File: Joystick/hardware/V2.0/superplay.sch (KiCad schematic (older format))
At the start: 36 parts, among them J1 AVR-PDI-6A, J2 CONN_02X04, J3 USB_B, U1 MCP1700T-3002E, U2 ATXMEGA128A3U-A, U3 TPD4S009DBV, Y1 16MHz

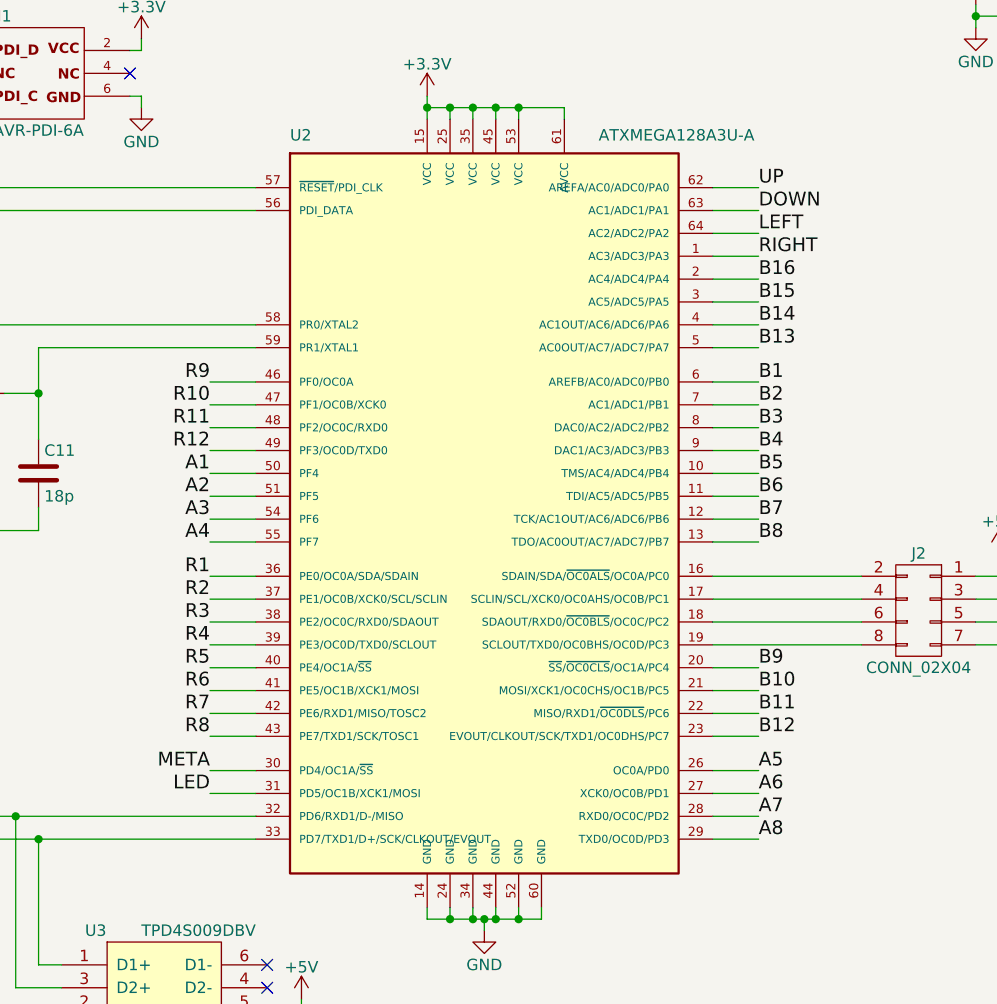
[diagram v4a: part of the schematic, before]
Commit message: Rewired to make PCB layout easier
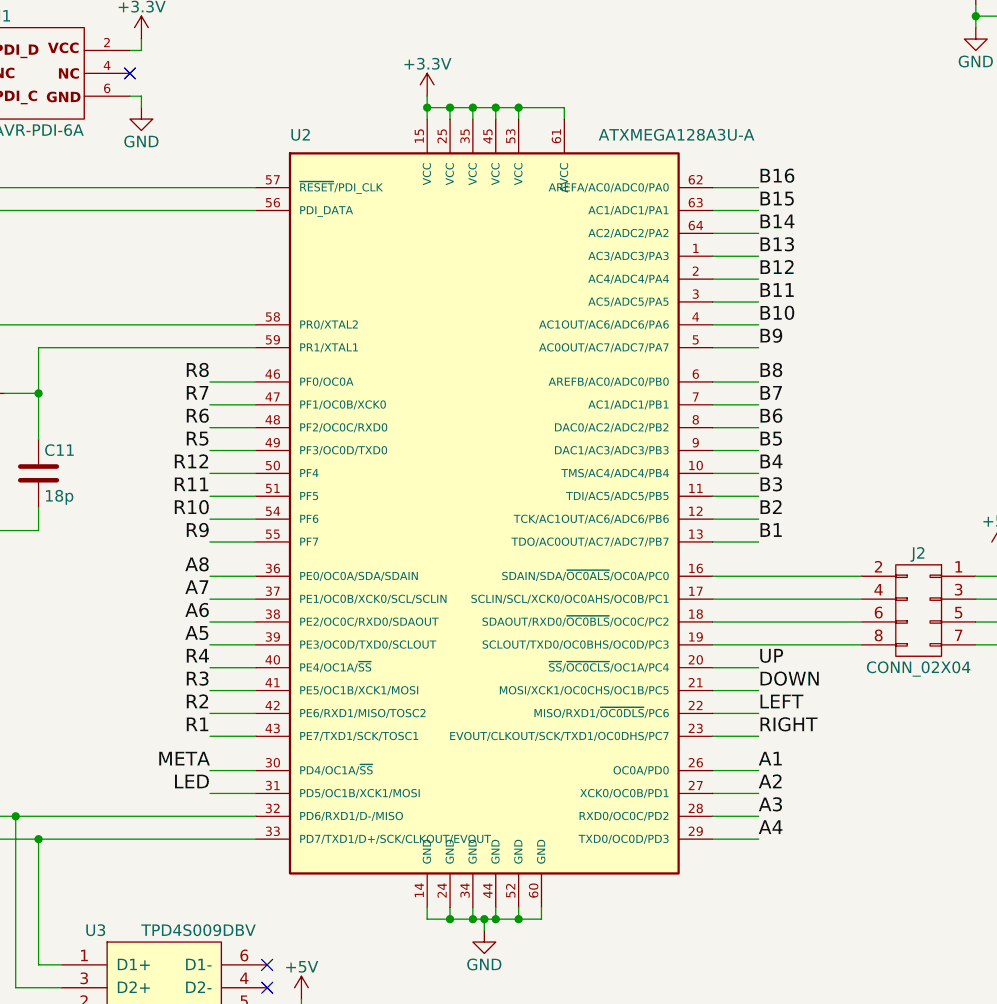
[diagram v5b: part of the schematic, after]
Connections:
- net A1: now also U2.26 (OC0A/PD0); no longer U2.50 (PF4)
- net A2: now also U2.27 (XCK0/OC0B/PD1); no longer U2.51 (PF5)
- net A3: now also U2.28 (RXD0/OC0C/PD2); no longer U2.54 (PF6)
- net A4: now also U2.29 (TXD0/OC0D/PD3); no longer U2.55 (PF7)
- net A5: now also U2.39 (PE3/OC0D/TXD0/SCLOUT); no longer U2.26 (OC0A/PD0)
- net A6: now also U2.38 (PE2/OC0C/RXD0/SDAOUT); no longer U2.27 (XCK0/OC0B/PD1)
- net A7: now also U2.37 (PE1/OC0B/XCK0/SCL/SCLIN); no longer U2.28 (RXD0/OC0C/PD2)
- net A8: now also U2.36 (PE0/OC0A/SDA/SDAIN); no longer U2.29 (TXD0/OC0D/PD3)
- net B1: now also U2.13 (TDO/AC0OUT/AC7/ADC7/PB7); no longer U2.6 (AREFB/AC0/ADC0/PB0)
- net B10: now also U2.4 (AC1OUT/AC6/ADC6/PA6); no longer U2.21 (MOSI/XCK1/OC0CHS/OC1B/PC5)
- net B11: now also U2.3 (AC5/ADC5/PA5); no longer U2.22 (MISO/RXD1/~OC0DLS~/PC6)
- net B12: now also U2.2 (AC4/ADC4/PA4); no longer U2.23 (EVOUT/CLKOUT/SCK/TXD1/OC0DHS/PC7)
- net B13: now also U2.1 (AC3/ADC3/PA3); no longer U2.5 (AC0OUT/AC7/ADC7/PA7)
- net B14: now also U2.64 (AC2/ADC2/PA2); no longer U2.4 (AC1OUT/AC6/ADC6/PA6)
- net B15: now also U2.63 (AC1/ADC1/PA1); no longer U2.3 (AC5/ADC5/PA5)
- net B16: now also U2.62 (AREFA/AC0/ADC0/PA0); no longer U2.2 (AC4/ADC4/PA4)
- net B2: now also U2.12 (TCK/AC1OUT/AC6/ADC6/PB6); no longer U2.7 (AC1/ADC1/PB1)
- net B3: now also U2.11 (TDI/AC5/ADC5/PB5); no longer U2.8 (DAC0/AC2/ADC2/PB2)
- net B4: now also U2.10 (TMS/AC4/ADC4/PB4); no longer U2.9 (DAC1/AC3/ADC3/PB3)
- net B5: now also U2.9 (DAC1/AC3/ADC3/PB3); no longer U2.10 (TMS/AC4/ADC4/PB4)
- net B6: now also U2.8 (DAC0/AC2/ADC2/PB2); no longer U2.11 (TDI/AC5/ADC5/PB5)
- net B7: now also U2.7 (AC1/ADC1/PB1); no longer U2.12 (TCK/AC1OUT/AC6/ADC6/PB6)
- net B8: now also U2.6 (AREFB/AC0/ADC0/PB0); no longer U2.13 (TDO/AC0OUT/AC7/ADC7/PB7)
- net B9: now also U2.5 (AC0OUT/AC7/ADC7/PA7); no longer U2.20 (~SS~/~OC0CLS~/OC1A/PC4)
- net DOWN: now also U2.21 (MOSI/XCK1/OC0CHS/OC1B/PC5); no longer U2.63 (AC1/ADC1/PA1)
- net LEFT: now also U2.22 (MISO/RXD1/~OC0DLS~/PC6); no longer U2.64 (AC2/ADC2/PA2)
- net R1: now also U2.43 (PE7/TXD1/SCK/TOSC1); no longer U2.36 (PE0/OC0A/SDA/SDAIN)
- net R10: now also U2.54 (PF6); no longer U2.47 (PF1/OC0B/XCK0)
- net R11: now also U2.51 (PF5); no longer U2.48 (PF2/OC0C/RXD0)
- net R12: now also U2.50 (PF4); no longer U2.49 (PF3/OC0D/TXD0)
- net R2: now also U2.42 (PE6/RXD1/MISO/TOSC2); no longer U2.37 (PE1/OC0B/XCK0/SCL/SCLIN)
- net R3: now also U2.41 (PE5/OC1B/XCK1/MOSI); no longer U2.38 (PE2/OC0C/RXD0/SDAOUT)
- net R4: now also U2.40 (PE4/OC1A/~SS~); no longer U2.39 (PE3/OC0D/TXD0/SCLOUT)
- net R5: now also U2.49 (PF3/OC0D/TXD0); no longer U2.40 (PE4/OC1A/~SS~)
- net R6: now also U2.48 (PF2/OC0C/RXD0); no longer U2.41 (PE5/OC1B/XCK1/MOSI)
- net R7: now also U2.47 (PF1/OC0B/XCK0); no longer U2.42 (PE6/RXD1/MISO/TOSC2)
- net R8: now also U2.46 (PF0/OC0A); no longer U2.43 (PE7/TXD1/SCK/TOSC1)
- net R9: now also U2.55 (PF7); no longer U2.46 (PF0/OC0A)
- net RIGHT: now also U2.23 (EVOUT/CLKOUT/SCK/TXD1/OC0DHS/PC7); no longer U2.1 (AC3/ADC3/PA3)
- net UP: now also U2.20 (~SS~/~OC0CLS~/OC1A/PC4); no longer U2.62 (AREFA/AC0/ADC0/PA0)
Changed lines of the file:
@@
 Connection ~ 9600 1250
 Wire Wire Line
+	5450 4100 5650 4100
+Wire Wire Line
+	5450 4200 5650 4200
+Wire Wire Line
+	5450 4300 5650 4300
+Wire Wire Line
+	5450 4400 5650 4400
+Wire Wire Line
 	5450 2000 5650 2000
 Wire Wire Line
@@
 	5450 2300 5650 2300
 Wire Wire Line
-	5450 2400 5650 2400
+	5450 2850 5650 2850
+Wire Wire Line
+	5450 2950 5650 2950
+Wire Wire Line
+	5450 3050 5650 3050
+Wire Wire Line
+	5450 3150 5650 3150
+Wire Wire Line
+	5450 3250 5650 3250
+Wire Wire Line
+	5450 3350 5650 3350
+Wire Wire Line
+	5450 3450 5650 3450
+Wire Wire Line
+	5450 3550 5650 3550
+Wire Wire Line
+	5450 2700 5650 2700
+Wire Wire Line
+	5450 2600 5650 2600
 Wire Wire Line
 	5450 2500 5650 2500
 Wire Wire Line
-	5450 2600 5650 2600
-Wire Wire Line
-	5450 2700 5650 2700
-Wire Wire Line
-	5450 2850 5650 2850
-Wire Wire Line
-	5450 2950 5650 2950
-Wire Wire Line
-	5450 3050 5650 3050
-Wire Wire Line
-	5450 3150 5650 3150
-Wire Wire Line
-	5450 3250 5650 3250
-Wire Wire Line
-	5450 3350 5650 3350
-Wire Wire Line
-	5450 3450 5650 3450
-Wire Wire Line
-	5450 3550 5650 3550
-Wire Wire Line
-	5450 4100 5650 4100
-Wire Wire Line
-	5450 4200 5650 4200
-Wire Wire Line
-	5450 4300 5650 4300
+	3450 4000 3250 4000
+Wire Wire Line
+	3450 3900 3250 3900
+Wire Wire Line
+	3450 3800 3250 3800
+Wire Wire Line
+	3450 3700 3250 3700
+Wire Wire Line
+	3450 3550 3250 3550
+Wire Wire Line
+	3450 3450 3250 3450
+Wire Wire Line
+	3450 3350 3250 3350
+Wire Wire Line
+	3450 3250 3250 3250
 Wire Wire Line
 	5450 4550 5650 4550
@@
 	5450 4850 5650 4850
 Wire Wire Line
+	3450 4400 3250 4400
+Wire Wire Line
+	3450 4300 3250 4300
+Wire Wire Line
+	3450 4200 3250 4200
+Wire Wire Line
+	3450 4100 3250 4100
+Wire Wire Line
+	3450 3150 3250 3150
+Wire Wire Line
+	3450 3050 3250 3050
+Wire Wire Line
+	3450 2950 3250 2950
+Wire Wire Line
 	3450 2850 3250 2850
-Wire Wire Line
-	3450 2950 3250 2950
-Wire Wire Line
-	3450 3050 3250 3050
-Wire Wire Line
-	3450 3150 3250 3150
-Wire Wire Line
-	3450 3250 3250 3250
-Wire Wire Line
-	3450 3350 3250 3350
-Wire Wire Line
-	3450 3450 3250 3450
-Wire Wire Line
-	3450 3550 3250 3550
-Wire Wire Line
-	3450 3700 3250 3700
-Wire Wire Line
-	3450 3800 3250 3800
-Wire Wire Line
-	3450 3900 3250 3900
-Wire Wire Line
-	3450 4000 3250 4000
-Wire Wire Line
-	3450 4100 3250 4100
-Wire Wire Line
-	3450 4200 3250 4200
-Wire Wire Line
-	3450 4300 3250 4300
-Wire Wire Line
-	3450 4400 3250 4400
 Wire Wire Line
 	3450 4550 3250 4550
@@
 	4450 5250 4450 5200
 Connection ~ 4450 5200
+Text Label 5650 4100 0    60   ~ 0
+UP
+Text Label 5650 4200 0    60   ~ 0
+DOWN
+Text Label 5650 4300 0    60   ~ 0
+LEFT
+Text Label 5650 4400 0    60   ~ 0
+RIGHT
 Text Label 5650 2000 0    60   ~ 0
-UP
+B16
 Text Label 5650 2100 0    60   ~ 0
-DOWN
+B15
 Text Label 5650 2200 0    60   ~ 0
-LEFT
+B14
 Text Label 5650 2300 0    60   ~ 0
-RIGHT
-Text Label 5650 2400 0    60   ~ 0
-B16
-Text Label 5650 2500 0    60   ~ 0
-B15
-Text Label 5650 2600 0    60   ~ 0
-B14
-Text Label 5650 2700 0    60   ~ 0
 B13
 Text Label 5650 2850 0    60   ~ 0
+B8
+Text Label 5650 2950 0    60   ~ 0
+B7
+Text Label 5650 3050 0    60   ~ 0
+B6
+Text Label 5650 3150 0    60   ~ 0
+B5
+Text Label 5650 3250 0    60   ~ 0
+B4
+Text Label 5650 3350 0    60   ~ 0
+B3
+Text Label 5650 3450 0    60   ~ 0
+B2
+Text Label 5650 3550 0    60   ~ 0
 B1
-Text Label 5650 2950 0    60   ~ 0
-B2
-Text Label 5650 3050 0    60   ~ 0
-B3
-Text Label 5650 3150 0    60   ~ 0
-B4
-Text Label 5650 3250 0    60   ~ 0
-B5
-Text Label 5650 3350 0    60   ~ 0
-B6
-Text Label 5650 3450 0    60   ~ 0
-B7
-Text Label 5650 3550 0    60   ~ 0
-B8
-Text Label 5650 4100 0    60   ~ 0
+Text Label 5650 2700 0    60   ~ 0
 B9
-Text Label 5650 4200 0    60   ~ 0
+Text Label 5650 2600 0    60   ~ 0
 B10
-Text Label 5650 4300 0    60   ~ 0
+Text Label 5650 2500 0    60   ~ 0
 B11
-Text Label 5650 4400 0    60   ~ 0
+Text Label 5650 2400 0    60   ~ 0
 B12
-Text Label 5650 4550 0    60   ~ 0
+Text Label 3250 4000 2    60   ~ 0
 A5
-Text Label 5650 4650 0    60   ~ 0
+Text Label 3250 3900 2    60   ~ 0
 A6
-Text Label 5650 4750 0    60   ~ 0
+Text Label 3250 3800 2    60   ~ 0
 A7
-Text Label 5650 4850 0    60   ~ 0
+Text Label 3250 3700 2    60   ~ 0
 A8
 Text Label 3250 4550 2    60   ~ 0
@@
 Text Label 3250 4650 2    60   ~ 0
 LED
-Text Label 3250 3700 2    60   ~ 0
+Text Label 3250 4400 2    60   ~ 0
 R1
-Text Label 3250 3800 2    60   ~ 0
+Text Label 3250 4300 2    60   ~ 0
 R2
-Text Label 3250 3900 2    60   ~ 0
+Text Label 3250 4200 2    60   ~ 0
 R3
-Text Label 3250 4000 2    60   ~ 0
+Text Label 3250 4100 2    60   ~ 0
 R4
-Text Label 3250 4100 2    60   ~ 0
+Text Label 3250 3150 2    60   ~ 0
 R5
-Text Label 3250 4200 2    60   ~ 0
+Text Label 3250 3050 2    60   ~ 0
 R6
-Text Label 3250 4300 2    60   ~ 0
+Text Label 3250 2950 2    60   ~ 0
 R7
-Text Label 3250 4400 2    60   ~ 0
+Text Label 3250 2850 2    60   ~ 0
 R8
-Text Label 3250 2850 2    60   ~ 0
+Text Label 3250 3550 2    60   ~ 0
 R9
-Text Label 3250 2950 2    60   ~ 0
+Text Label 3250 3450 2    60   ~ 0
 R10
-Text Label 3250 3050 2    60   ~ 0
+Text Label 3250 3350 2    60   ~ 0
 R11
-Text Label 3250 3150 2    60   ~ 0
+Text Label 3250 3250 2    60   ~ 0
 R12
-Text Label 3250 3250 2    60   ~ 0
+Text Label 5650 4550 0    60   ~ 0
 A1
-Text Label 3250 3350 2    60   ~ 0
+Text Label 5650 4650 0    60   ~ 0
 A2
-Text Label 3250 3450 2    60   ~ 0
+Text Label 5650 4750 0    60   ~ 0
 A3
-Text Label 3250 3550 2    60   ~ 0
+Text Label 5650 4850 0    60   ~ 0
 A4
 Wire Wire Line
@@
 Connection ~ 1900 2900
 Wire Wire Line
-	5650 4400 5450 4400
+	5650 2400 5450 2400
 Wire Wire Line
 	6100 4000 5450 4000
@@
 $EndComp
 $Comp
-L GND #PWR?
+L GND #PWR032
 U 1 1 5918CADC
 P 1300 6950
-F 0 "#PWR?" H 1300 6700 50  0001 C CNN
+F 0 "#PWR032" H 1300 6700 50  0001 C CNN
 F 1 "GND" H 1300 6800 50  0000 C CNN
 F 2 "" H 1300 6950 50  0000 C CNN
@@
 $EndComp
 $Comp
-L GND #PWR?
+L GND #PWR033
 U 1 1 5918CB53
 P 1650 6950
-F 0 "#PWR?" H 1650 6700 50  0001 C CNN
+F 0 "#PWR033" H 1650 6700 50  0001 C CNN
 F 1 "GND" H 1650 6800 50  0000 C CNN
 F 2 "" H 1650 6950 50  0000 C CNN
@@
 $EndComp
 $Comp
-L GND #PWR?
+L GND #PWR034
 U 1 1 5918CBCA
 P 2000 6950
-F 0 "#PWR?" H 2000 6700 50  0001 C CNN
+F 0 "#PWR034" H 2000 6700 50  0001 C CNN
 F 1 "GND" H 2000 6800 50  0000 C CNN
 F 2 "" H 2000 6950 50  0000 C CNN
@@
 $EndComp
 $Comp
-L GND #PWR?
+L GND #PWR035
 U 1 1 5918CC41
 P 2350 6950
-F 0 "#PWR?" H 2350 6700 50  0001 C CNN
+F 0 "#PWR035" H 2350 6700 50  0001 C CNN
 F 1 "GND" H 2350 6800 50  0000 C CNN
 F 2 "" H 2350 6950 50  0000 C CNN

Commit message: Routing looks successful
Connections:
- net A1: now also U2.31 (PD5/OC1B/XCK1/MOSI); no longer U2.26 (OC0A/PD0)
- net A2: now also U2.30 (PD4/OC1A/~SS~); no longer U2.27 (XCK0/OC0B/PD1)
- net A3: now also U2.29 (TXD0/OC0D/PD3); no longer U2.28 (RXD0/OC0C/PD2)
- net A4: now also U2.28 (RXD0/OC0C/PD2); no longer U2.29 (TXD0/OC0D/PD3)
- net LED: now also U2.27 (XCK0/OC0B/PD1); no longer U2.31 (PD5/OC1B/XCK1/MOSI)
- net META: now also U2.26 (OC0A/PD0); no longer U2.30 (PD4/OC1A/~SS~)
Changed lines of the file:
@@
 	3450 3250 3250 3250
 Wire Wire Line
-	5450 4550 5650 4550
+	3450 4650 3250 4650
 Wire Wire Line
-	5450 4650 5650 4650
+	3450 4550 3250 4550
+Wire Wire Line
+	5450 4850 5650 4850
 Wire Wire Line
 	5450 4750 5650 4750
-Wire Wire Line
-	5450 4850 5650 4850
 Wire Wire Line
 	3450 4400 3250 4400
@@
 	3450 2850 3250 2850
 Wire Wire Line
-	3450 4550 3250 4550
+	5450 4550 5650 4550
 Wire Wire Line
-	3450 4650 3250 4650
+	5450 4650 5650 4650
 Wire Wire Line
 	2000 4750 3450 4750
@@
 Text Label 3250 3700 2    60   ~ 0
 A8
-Text Label 3250 4550 2    60   ~ 0
+Text Label 5650 4550 0    60   ~ 0
 META
-Text Label 3250 4650 2    60   ~ 0
+Text Label 5650 4650 0    60   ~ 0
 LED
 Text Label 3250 4400 2    60   ~ 0
@@
 Text Label 3250 3250 2    60   ~ 0
 R12
-Text Label 5650 4550 0    60   ~ 0
+Text Label 3250 4650 2    60   ~ 0
 A1
-Text Label 5650 4650 0    60   ~ 0
+Text Label 3250 4550 2    60   ~ 0
 A2
+Text Label 5650 4850 0    60   ~ 0
+A3
 Text Label 5650 4750 0    60   ~ 0
-A3
-Text Label 5650 4850 0    60   ~ 0
 A4
 Wire Wire Line

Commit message: Upgraded to Kicad 4.0.7
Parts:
- J3: symbol USB_B -> USB_B-RESCUE-superplay
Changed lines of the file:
@@
 EESchema Schematic File Version 2
+LIBS:superplay-rescue
 LIBS:power
 LIBS:device
@@
 $EndComp
 $Comp
-L USB_B J3
+L USB_B-RESCUE-superplay J3
 U 1 1 59143165
 P 1700 4850
